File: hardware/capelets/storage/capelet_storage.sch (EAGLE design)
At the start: 4 parts

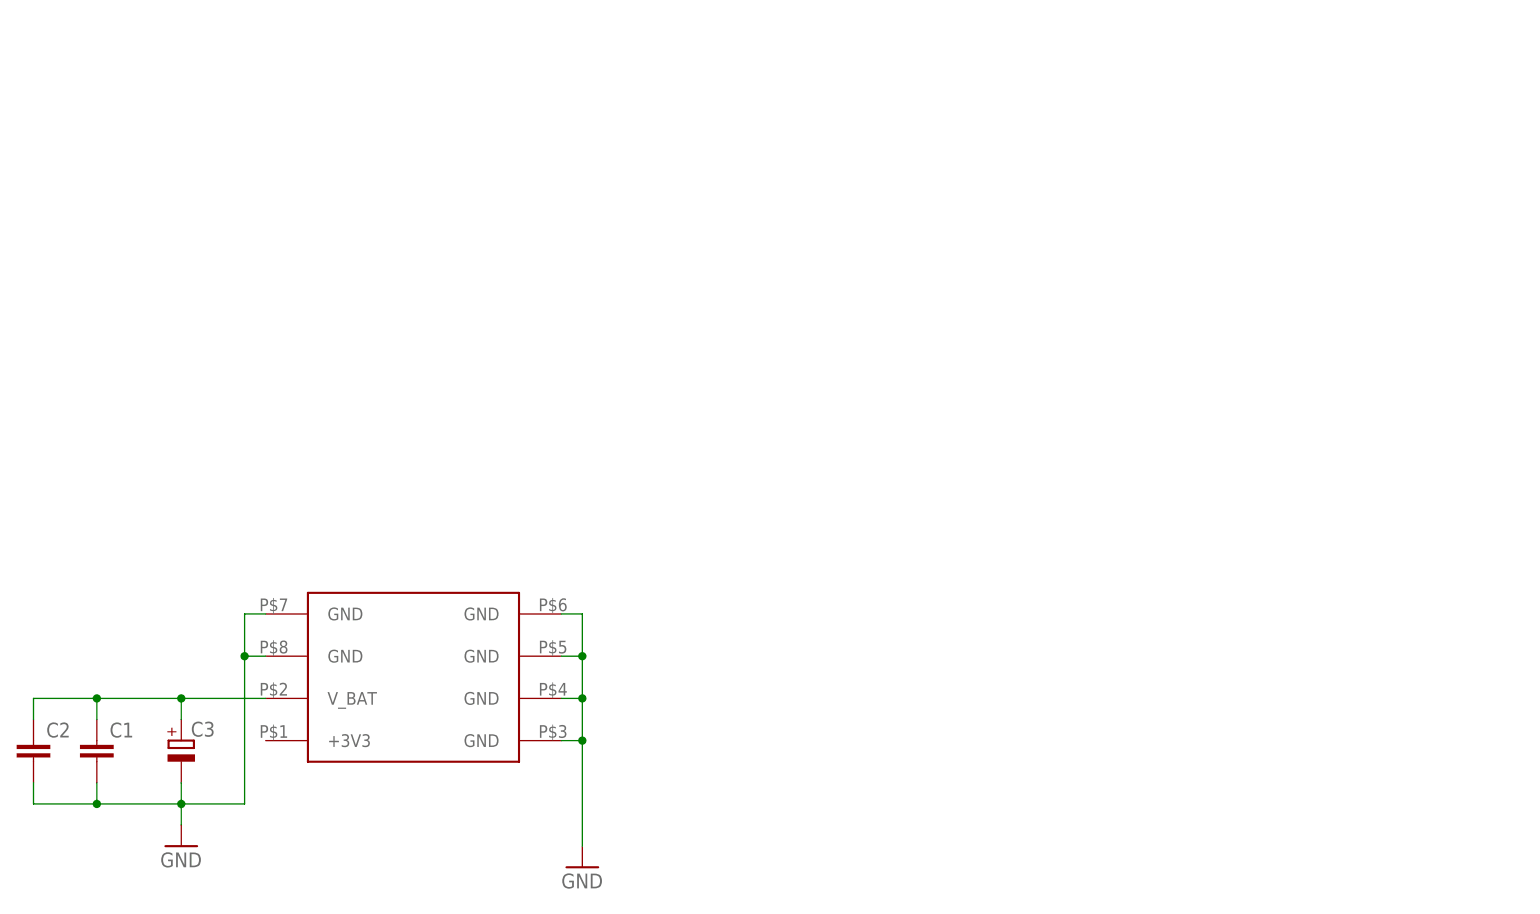
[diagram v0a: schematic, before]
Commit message: hardware: fancy frames around capelet schematics
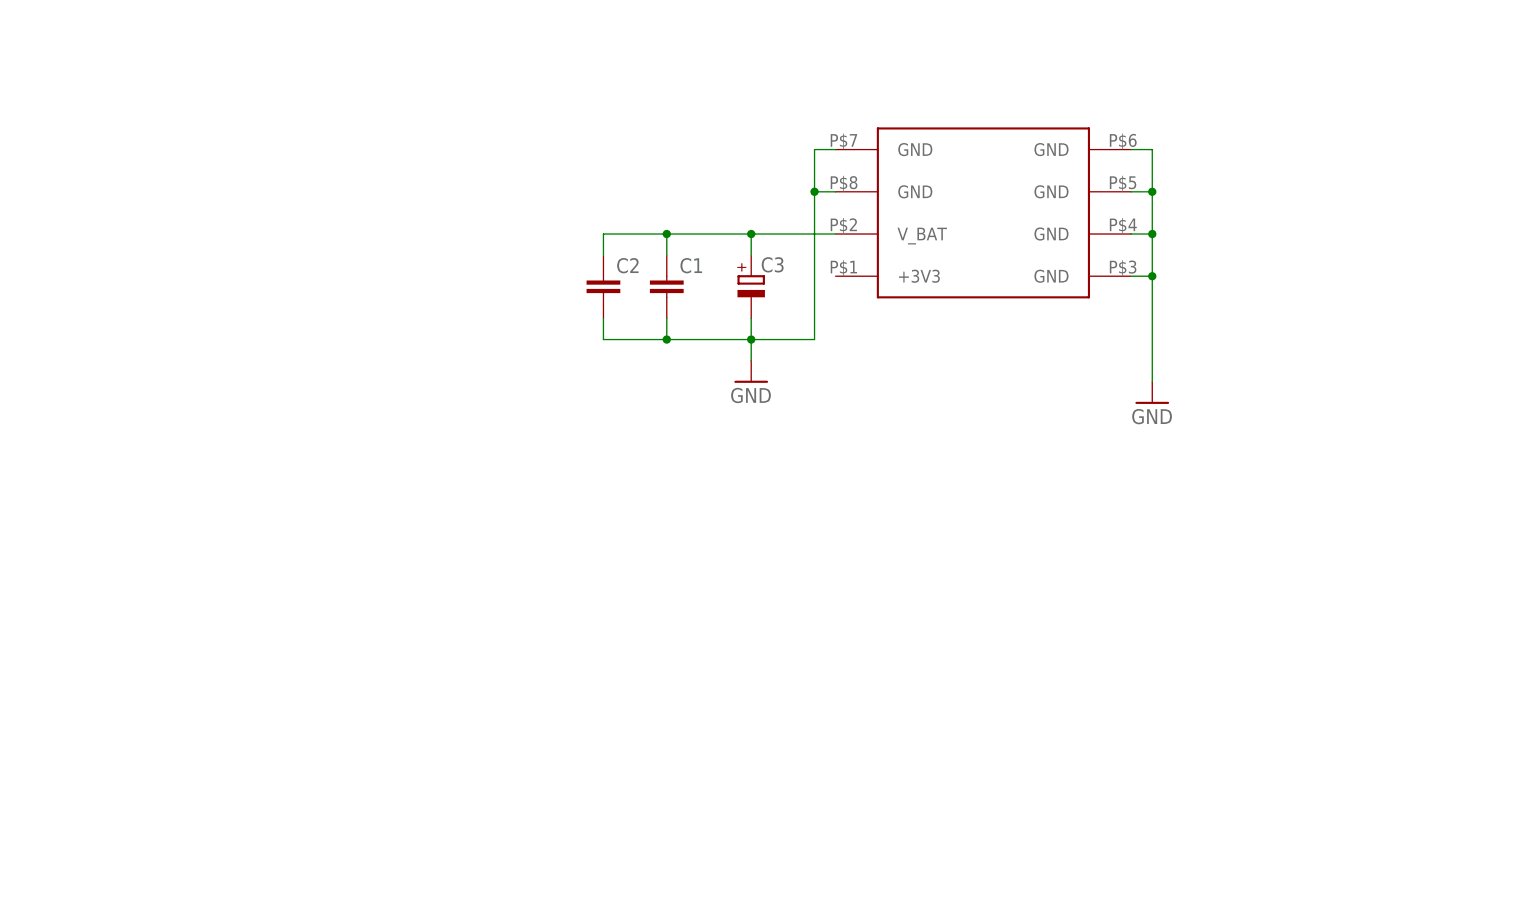
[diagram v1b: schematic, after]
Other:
- moved on the sheet: C1, C2, C3
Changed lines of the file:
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@@
 <part name="GND1" library="supply1" library_urn="urn:adsk.eagle:library:371" deviceset="GND" device=""/>
 <part name="GND2" library="supply1" library_urn="urn:adsk.eagle:library:371" deviceset="GND" device=""/>
+<part name="FRAME1" library="frames" library_urn="urn:adsk.eagle:library:229" deviceset="A4L-LOC" device=""/>
 </parts>
 <sheets>
@@
 </plain>
 <instances>
-<instance part="U$1" gate="G$1" x="2.54" y="-2.54" smashed="yes"/>
-<instance part="C1" gate="G$1" x="-17.78" y="2.54" smashed="yes">
-<attribute name="NAME" x="-16.256" y="2.921" size="1.778" layer="95"/>
-<attribute name="VALUE" x="-16.256" y="-2.159" size="1.778" layer="96"/>
+<instance part="U$1" gate="G$1" x="71.12" y="53.34" smashed="yes"/>
+<instance part="C1" gate="G$1" x="50.8" y="58.42" smashed="yes">
+<attribute name="NAME" x="52.324" y="58.801" size="1.778" layer="95"/>
+<attribute name="VALUE" x="52.324" y="53.721" size="1.778" layer="96"/>
 </instance>
-<instance part="C2" gate="G$1" x="-25.4" y="2.54" smashed="yes">
-<attribute name="NAME" x="-23.876" y="2.921" size="1.778" layer="95"/>
-<attribute name="VALUE" x="-23.876" y="-2.159" size="1.778" layer="96"/>
+<instance part="C2" gate="G$1" x="43.18" y="58.42" smashed="yes">
+<attribute name="NAME" x="44.704" y="58.801" size="1.778" layer="95"/>
+<attribute name="VALUE" x="44.704" y="53.721" size="1.778" layer="96"/>
 </instance>
-<instance part="C3" gate="G$1" x="-7.62" y="2.54" smashed="yes">
-<attribute name="NAME" x="-6.477" y="3.0226" size="1.778" layer="95"/>
-<attribute name="VALUE" x="-6.477" y="-2.0574" size="1.778" layer="96"/>
+<instance part="C3" gate="G$1" x="60.96" y="58.42" smashed="yes">
+<attribute name="NAME" x="62.103" y="58.9026" size="1.778" layer="95"/>
+<attribute name="VALUE" x="62.103" y="53.8226" size="1.778" layer="96"/>
 </instance>
-<instance part="GND1" gate="1" x="-7.62" y="-10.16" smashed="yes">
-<attribute name="VALUE" x="-10.16" y="-12.7" size="1.778" layer="96"/>
+<instance part="GND1" gate="1" x="60.96" y="45.72" smashed="yes">
+<attribute name="VALUE" x="58.42" y="43.18" size="1.778" layer="96"/>
 </instance>
-<instance part="GND2" gate="1" x="40.64" y="-12.7" smashed="yes">
-<attribute name="VALUE" x="38.1" y="-15.24" size="1.778" layer="96"/>
+<instance part="GND2" gate="1" x="109.22" y="43.18" smashed="yes">
+<attribute name="VALUE" x="106.68" y="40.64" size="1.778" layer="96"/>
+</instance>
+<instance part="FRAME1" gate="G$1" x="0" y="0" smashed="yes">
+<attribute name="DRAWING_NAME" x="217.17" y="15.24" size="2.54" layer="94"/>
+<attribute name="LAST_DATE_TIME" x="217.17" y="10.16" size="2.286" layer="94"/>
+<attribute name="SHEET" x="230.505" y="5.08" size="2.54" layer="94"/>
 </instance>
 </instances>
@@
 <pinref part="C2" gate="G$1" pin="1"/>
 <pinref part="U$1" gate="G$1" pin="V_BAT"/>
-<wire x1="-25.4" y1="5.08" x2="-25.4" y2="7.62" width="0.1524" layer="91"/>
-<wire x1="-25.4" y1="7.62" x2="-17.78" y2="7.62" width="0.1524" layer="91"/>
+<wire x1="43.18" y1="60.96" x2="43.18" y2="63.5" width="0.1524" layer="91"/>
+<wire x1="43.18" y1="63.5" x2="50.8" y2="63.5" width="0.1524" layer="91"/>
 <pinref part="C1" gate="G$1" pin="1"/>
-<wire x1="-17.78" y1="7.62" x2="-7.62" y2="7.62" width="0.1524" layer="91"/>
-<wire x1="-7.62" y1="7.62" x2="2.54" y2="7.62" width="0.1524" layer="91"/>
-<wire x1="-17.78" y1="5.08" x2="-17.78" y2="7.62" width="0.1524" layer="91"/>
-<junction x="-17.78" y="7.62"/>
+<wire x1="50.8" y1="63.5" x2="60.96" y2="63.5" width="0.1524" layer="91"/>
+<wire x1="60.96" y1="63.5" x2="71.12" y2="63.5" width="0.1524" layer="91"/>
+<wire x1="50.8" y1="60.96" x2="50.8" y2="63.5" width="0.1524" layer="91"/>
+<junction x="50.8" y="63.5"/>
 <pinref part="C3" gate="G$1" pin="+"/>
-<wire x1="-7.62" y1="5.08" x2="-7.62" y2="7.62" width="0.1524" layer="91"/>
-<junction x="-7.62" y="7.62"/>
+<wire x1="60.96" y1="60.96" x2="60.96" y2="63.5" width="0.1524" layer="91"/>
+<junction x="60.96" y="63.5"/>
 </segment>
 </net>
@@
 <pinref part="GND1" gate="1" pin="GND"/>
 <pinref part="C3" gate="G$1" pin="-"/>
-<wire x1="-7.62" y1="-7.62" x2="-7.62" y2="-5.08" width="0.1524" layer="91"/>
+<wire x1="60.96" y1="48.26" x2="60.96" y2="50.8" width="0.1524" layer="91"/>
 <pinref part="C1" gate="G$1" pin="2"/>
-<wire x1="-7.62" y1="-5.08" x2="-7.62" y2="-2.54" width="0.1524" layer="91"/>
-<wire x1="-17.78" y1="-2.54" x2="-17.78" y2="-5.08" width="0.1524" layer="91"/>
-<wire x1="-17.78" y1="-5.08" x2="-7.62" y2="-5.08" width="0.1524" layer="91"/>
-<junction x="-7.62" y="-5.08"/>
+<wire x1="60.96" y1="50.8" x2="60.96" y2="53.34" width="0.1524" layer="91"/>
+<wire x1="50.8" y1="53.34" x2="50.8" y2="50.8" width="0.1524" layer="91"/>
+<wire x1="50.8" y1="50.8" x2="60.96" y2="50.8" width="0.1524" layer="91"/>
+<junction x="60.96" y="50.8"/>
 <pinref part="C2" gate="G$1" pin="2"/>
-<wire x1="-25.4" y1="-2.54" x2="-25.4" y2="-5.08" width="0.1524" layer="91"/>
-<wire x1="-25.4" y1="-5.08" x2="-17.78" y2="-5.08" width="0.1524" layer="91"/>
-<junction x="-17.78" y="-5.08"/>
-<wire x1="-7.62" y1="-5.08" x2="0" y2="-5.08" width="0.1524" layer="91"/>
-<wire x1="0" y1="-5.08" x2="0" y2="12.7" width="0.1524" layer="91"/>
+<wire x1="43.18" y1="53.34" x2="43.18" y2="50.8" width="0.1524" layer="91"/>
+<wire x1="43.18" y1="50.8" x2="50.8" y2="50.8" width="0.1524" layer="91"/>
+<junction x="50.8" y="50.8"/>
+<wire x1="60.96" y1="50.8" x2="68.58" y2="50.8" width="0.1524" layer="91"/>
+<wire x1="68.58" y1="50.8" x2="68.58" y2="68.58" width="0.1524" layer="91"/>
 <pinref part="U$1" gate="G$1" pin="GND@1"/>
-<wire x1="0" y1="12.7" x2="2.54" y2="12.7" width="0.1524" layer="91"/>
+<wire x1="68.58" y1="68.58" x2="71.12" y2="68.58" width="0.1524" layer="91"/>
 <pinref part="U$1" gate="G$1" pin="GND@2"/>
-<wire x1="0" y1="12.7" x2="0" y2="17.78" width="0.1524" layer="91"/>
-<wire x1="0" y1="17.78" x2="2.54" y2="17.78" width="0.1524" layer="91"/>
-<junction x="0" y="12.7"/>
+<wire x1="68.58" y1="68.58" x2="68.58" y2="73.66" width="0.1524" layer="91"/>
+<wire x1="68.58" y1="73.66" x2="71.12" y2="73.66" width="0.1524" layer="91"/>
+<junction x="68.58" y="68.58"/>
 </segment>
 <segment>
 <pinref part="GND2" gate="1" pin="GND"/>
 <pinref part="U$1" gate="G$1" pin="GND@3"/>
-<wire x1="40.64" y1="-10.16" x2="40.64" y2="2.54" width="0.1524" layer="91"/>
-<wire x1="40.64" y1="2.54" x2="40.64" y2="7.62" width="0.1524" layer="91"/>
-<wire x1="40.64" y1="7.62" x2="40.64" y2="12.7" width="0.1524" layer="91"/>
-<wire x1="40.64" y1="12.7" x2="40.64" y2="17.78" width="0.1524" layer="91"/>
-<wire x1="40.64" y1="17.78" x2="38.1" y2="17.78" width="0.1524" layer="91"/>
+<wire x1="109.22" y1="45.72" x2="109.22" y2="58.42" width="0.1524" layer="91"/>
+<wire x1="109.22" y1="58.42" x2="109.22" y2="63.5" width="0.1524" layer="91"/>
+<wire x1="109.22" y1="63.5" x2="109.22" y2="68.58" width="0.1524" layer="91"/>
+<wire x1="109.22" y1="68.58" x2="109.22" y2="73.66" width="0.1524" layer="91"/>
+<wire x1="109.22" y1="73.66" x2="106.68" y2="73.66" width="0.1524" layer="91"/>
 <pinref part="U$1" gate="G$1" pin="GND@4"/>
-<wire x1="38.1" y1="12.7" x2="40.64" y2="12.7" width="0.1524" layer="91"/>
-<junction x="40.64" y="12.7"/>
+<wire x1="106.68" y1="68.58" x2="109.22" y2="68.58" width="0.1524" layer="91"/>
+<junction x="109.22" y="68.58"/>
 <pinref part="U$1" gate="G$1" pin="GND@5"/>
-<wire x1="38.1" y1="7.62" x2="40.64" y2="7.62" width="0.1524" layer="91"/>
-<junction x="40.64" y="7.62"/>
+<wire x1="106.68" y1="63.5" x2="109.22" y2="63.5" width="0.1524" layer="91"/>
+<junction x="109.22" y="63.5"/>
 <pinref part="U$1" gate="G$1" pin="GND@6"/>
-<wire x1="38.1" y1="2.54" x2="40.64" y2="2.54" width="0.1524" layer="91"/>
-<junction x="40.64" y="2.54"/>
+<wire x1="106.68" y1="58.42" x2="109.22" y2="58.42" width="0.1524" layer="91"/>
+<junction x="109.22" y="58.42"/>
 </segment>
 </net>
